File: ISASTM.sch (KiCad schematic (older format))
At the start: 137 parts, among them J1 Bus_ISA_8bit, J2 USB_C_Receptacle_USB2.0, J3 Boot select, J4 USB_C_Receptacle_USB2.0, J5 TagConnect_TC2030_SWD, SW1 Reset, U1 STM32H743IITx, U10 SN74AVC8T245PW, U11 SN74AVC8T245PW, U12 SN74AVC8T245PW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

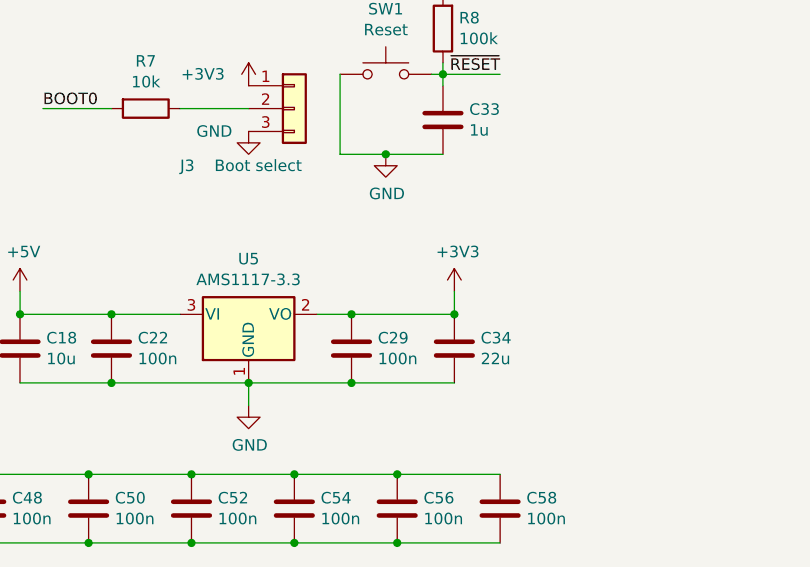
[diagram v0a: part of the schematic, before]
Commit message: Add 3v3 testpoint
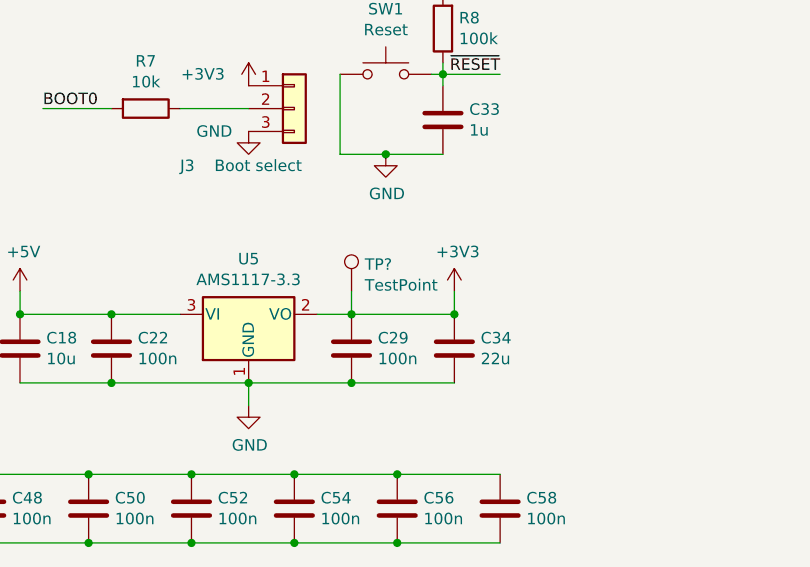
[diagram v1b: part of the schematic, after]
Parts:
- added TP?: TestPoint, TestPoint:TestPoint_Pad_2.0x2.0mm, symbol Connector:TestPoint
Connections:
- net +3V3: now also TP?.1
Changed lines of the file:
@@
 Text Label 1450 5400 0    50   ~ 0
 ~SPARE1_OE
+$Comp
+L Connector:TestPoint TP?
+U 1 1 625A8D11
+P 21850 10600
+F 0 "TP?" H 21908 10718 50  0000 L CNN
+F 1 "TestPoint" H 21908 10627 50  0000 L CNN
+F 2 "TestPoint:TestPoint_Pad_2.0x2.0mm" H 22050 10600 50  0001 C CNN
+F 3 "~" H 22050 10600 50  0001 C CNN
+	1    21850 10600
+	1    0    0    -1
+$EndComp
+Wire Wire Line
+	21850 10600 21850 10700
 $EndSCHEMATC

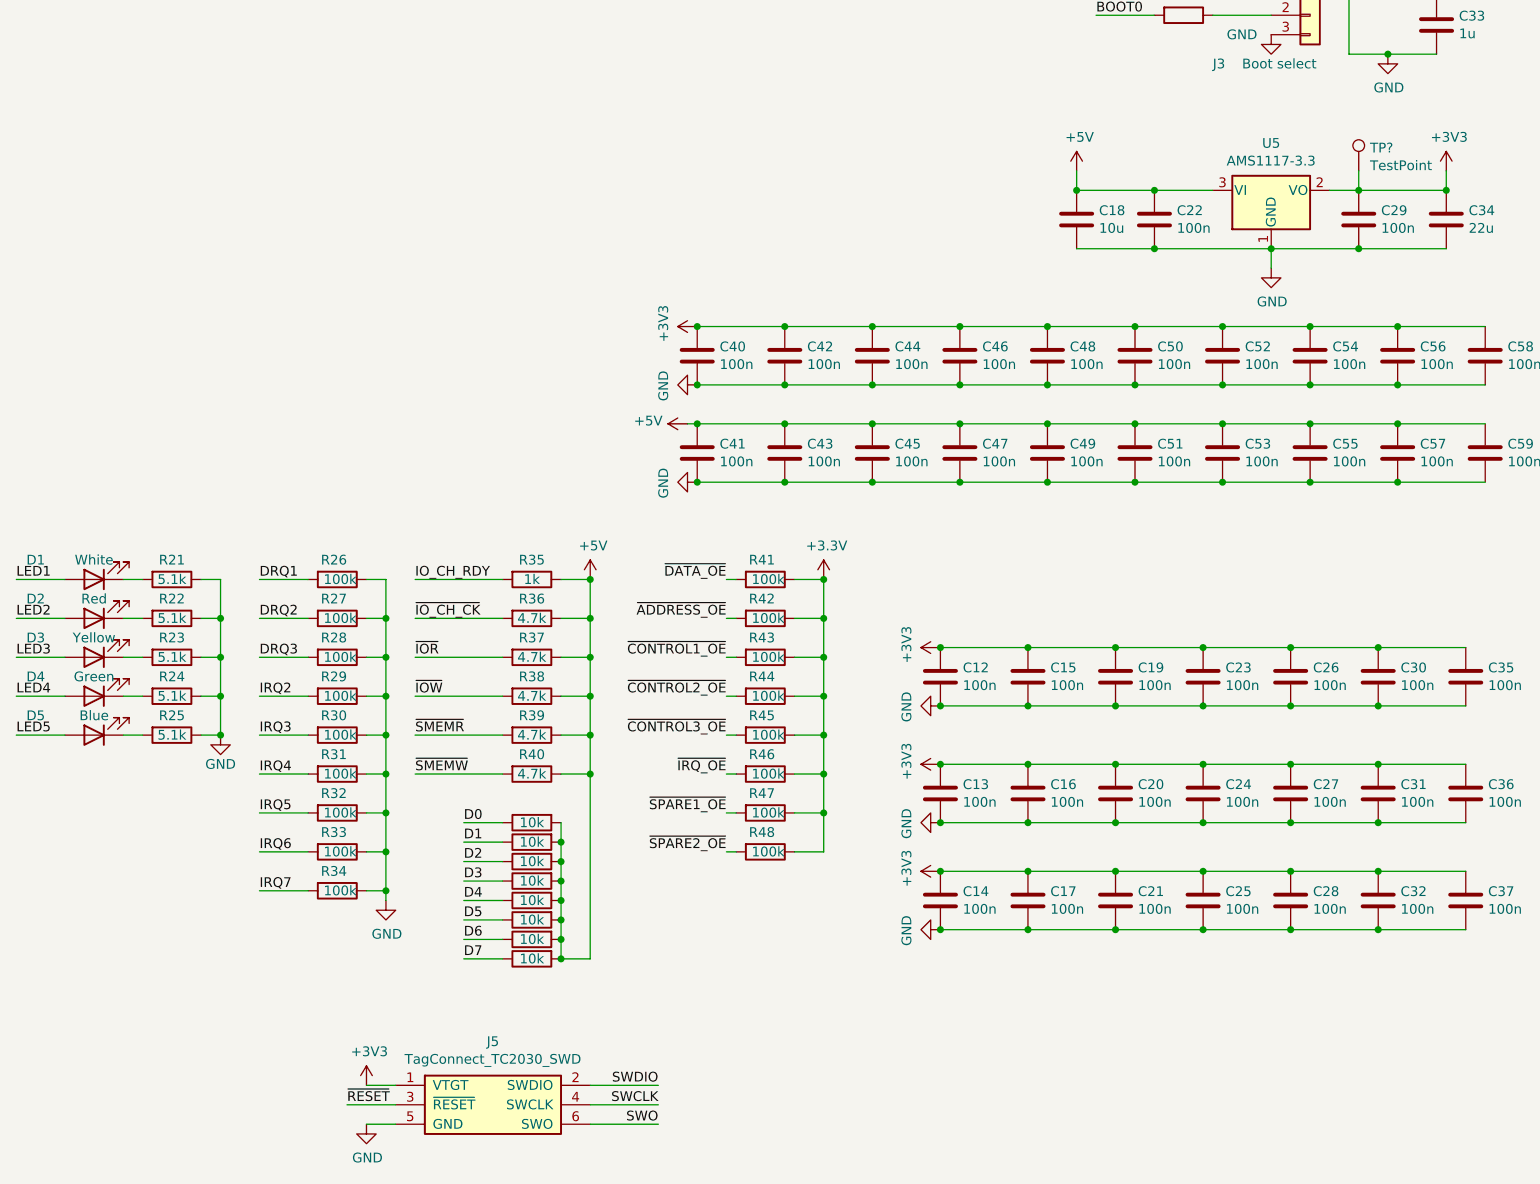
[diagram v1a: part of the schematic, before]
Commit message: Add tooling holes
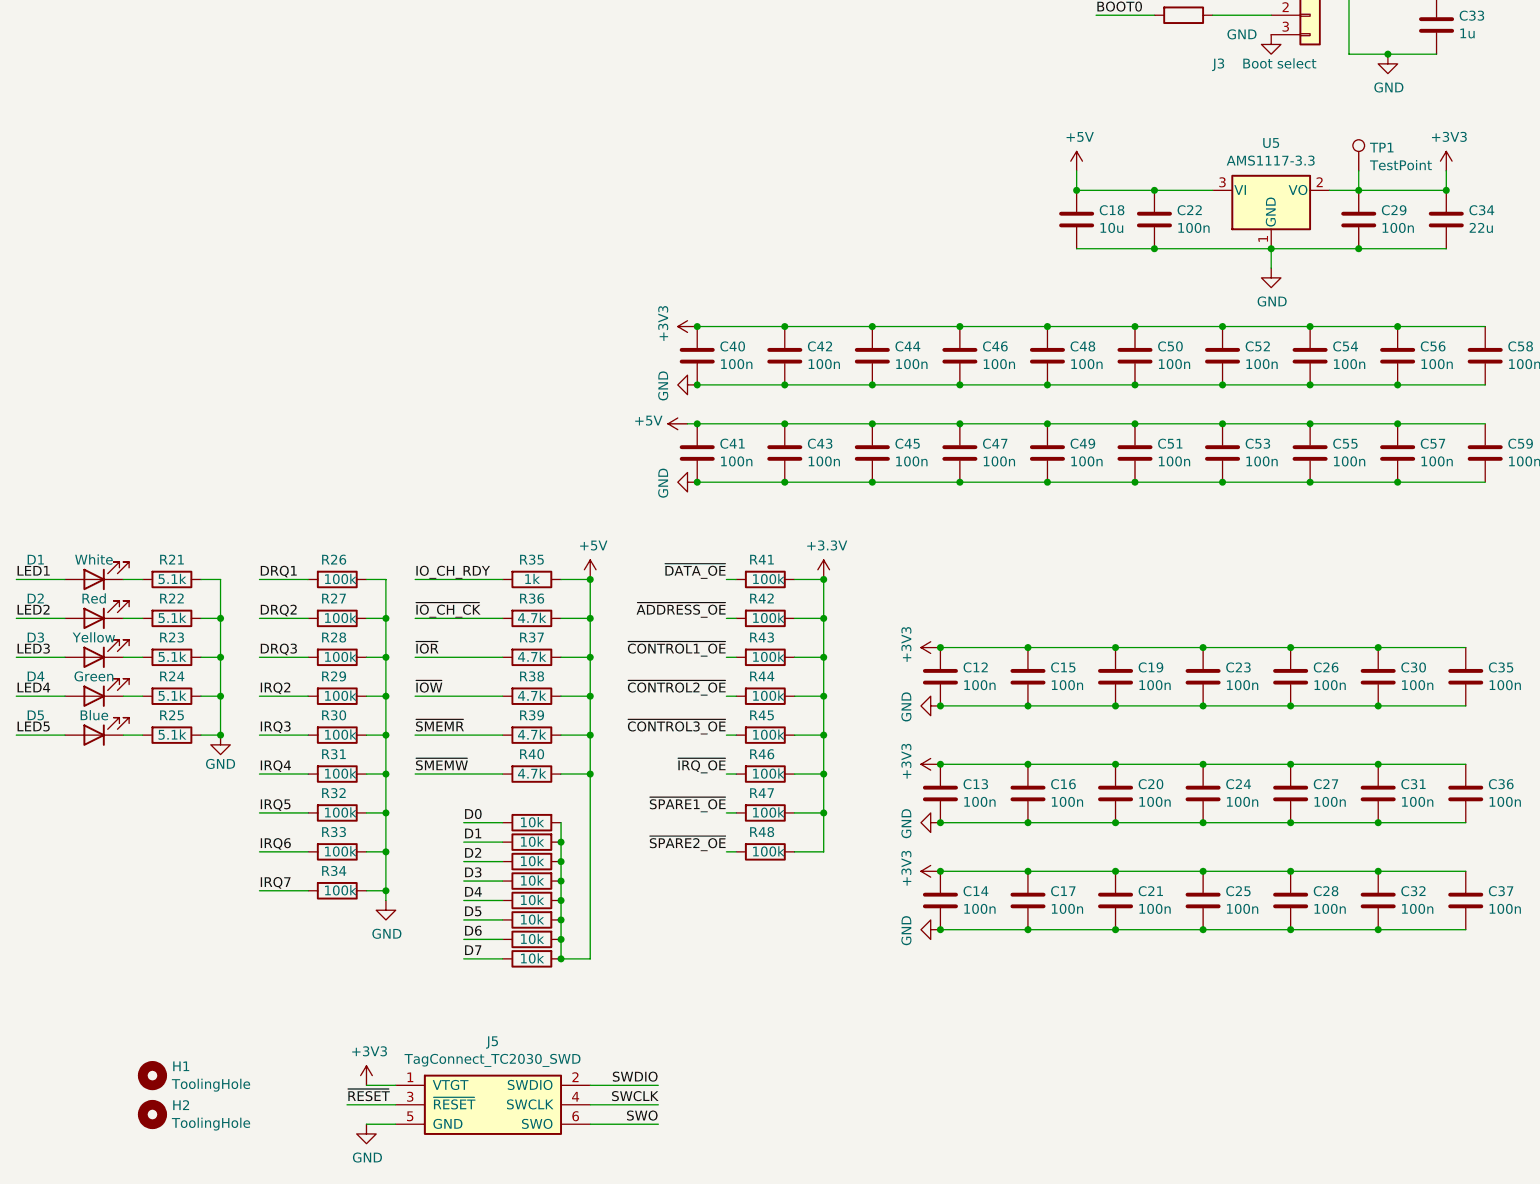
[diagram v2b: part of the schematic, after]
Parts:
- added H1, H2: ToolingHole, ISASTM:ToolingHole_JLCSMT, symbol Mechanical:MountingHole
- gave numbers to parts that had none: 1
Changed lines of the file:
@@
 ~SPARE1_OE
 $Comp
-L Connector:TestPoint TP?
+L Connector:TestPoint TP1
 U 1 1 625A8D11
 P 21850 10600
-F 0 "TP?" H 21908 10718 50  0000 L CNN
+F 0 "TP1" H 21908 10718 50  0000 L CNN
 F 1 "TestPoint" H 21908 10627 50  0000 L CNN
 F 2 "TestPoint:TestPoint_Pad_2.0x2.0mm" H 22050 10600 50  0001 C CNN
@@
 Wire Wire Line
 	21850 10600 21850 10700
+$Comp
+L Mechanical:MountingHole H1
+U 1 1 626BAFD0
+P 15650 15250
+F 0 "H1" H 15750 15296 50  0000 L CNN
+F 1 "ToolingHole" H 15750 15205 50  0000 L CNN
+F 2 "ISASTM:ToolingHole_JLCSMT" H 15650 15250 50  0001 C CNN
+F 3 "~" H 15650 15250 50  0001 C CNN
+	1    15650 15250
+	1    0    0    -1
+$EndComp
+$Comp
+L Mechanical:MountingHole H2
+U 1 1 5F7A598D
+P 15650 15450
+F 0 "H2" H 15750 15496 50  0000 L CNN
+F 1 "ToolingHole" H 15750 15405 50  0000 L CNN
+F 2 "ISASTM:ToolingHole_JLCSMT" H 15650 15450 50  0001 C CNN
+F 3 "~" H 15650 15450 50  0001 C CNN
+	1    15650 15450
+	1    0    0    -1
+$EndComp
 $EndSCHEMATC

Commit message: Fix missing ~REFRESH resistor, add better renders
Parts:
- added R49: 4.7k, Resistor_SMD:R_0402_1005Metric, symbol Device:R
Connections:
- net +5V: now also R49.1
- net ~REFRESH: now also R49.2
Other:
- note removed: "Refresh-Leitung braucht Pullup (und ist theoretisch bidirektional)\n"
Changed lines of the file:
@@
 Wire Wire Line
 	17450 4550 17950 4550
-Text Notes 23550 4250 0    197  ~ 0
-Refresh-Leitung braucht Pullup (und ist theoretisch bidirektional)\n
-Text Label 17250 14650 0    50   ~ 0
+Text Label 17250 14750 0    50   ~ 0
 D7
-Text Label 17250 14550 0    50   ~ 0
+Text Label 17250 14650 0    50   ~ 0
 D6
-Text Label 17250 14450 0    50   ~ 0
+Text Label 17250 14550 0    50   ~ 0
 D5
-Text Label 17250 14350 0    50   ~ 0
+Text Label 17250 14450 0    50   ~ 0
 D4
-Text Label 17250 14250 0    50   ~ 0
+Text Label 17250 14350 0    50   ~ 0
 D3
-Text Label 17250 14150 0    50   ~ 0
+Text Label 17250 14250 0    50   ~ 0
 D2
-Text Label 17250 14050 0    50   ~ 0
+Text Label 17250 14150 0    50   ~ 0
 D1
-Text Label 17250 13950 0    50   ~ 0
+Text Label 17250 14050 0    50   ~ 0
 D0
 Wire Wire Line
-	17450 13950 17250 13950
-Wire Wire Line
-	17250 14050 17450 14050
+	17450 14050 17250 14050
 Wire Wire Line
-	17450 14150 17250 14150
+	17250 14150 17450 14150
 Wire Wire Line
 	17450 14250 17250 14250
 Wire Wire Line
-	17250 14350 17450 14350
+	17450 14350 17250 14350
 Wire Wire Line
-	17450 14450 17250 14450
+	17250 14450 17450 14450
 Wire Wire Line
-	17250 14550 17450 14550
+	17450 14550 17250 14550
 Wire Wire Line
-	17450 14650 17250 14650
+	17250 14650 17450 14650
+Wire Wire Line
+	17450 14750 17250 14750
 $Comp
 L Device:R R?
 U 1 1 60585D61
-P 17600 13950
+P 17600 14050
 AR Path="/5F65970E/60585D61" Ref="R?"  Part="1"
 AR Path="/60585D61" Ref="R3"  Part="1"
-F 0 "R3" V 17393 13950 50  0001 C CNN
-F 1 "10k" V 17600 13950 50  0000 C CNN
-F 2 "Resistor_SMD:R_0402_1005Metric" V 17530 13950 50  0001 C CNN
-F 3 "~" H 17600 13950 50  0001 C CNN
-F 4 "C25744" V 17600 13950 50  0001 C CNN "LCSC"
-	1    17600 13950
-	0    -1   1    0
-$EndComp
-$Comp
-L Device:R R?
-U 1 1 6064A041
-P 17600 14050
-AR Path="/5F65970E/6064A041" Ref="R?"  Part="1"
-AR Path="/6064A041" Ref="R4"  Part="1"
-F 0 "R4" V 17393 14050 50  0001 C CNN
+F 0 "R3" V 17393 14050 50  0001 C CNN
 F 1 "10k" V 17600 14050 50  0000 C CNN
 F 2 "Resistor_SMD:R_0402_1005Metric" V 17530 14050 50  0001 C CNN
@@
 $Comp
 L Device:R R?
-U 1 1 606AB35D
+U 1 1 6064A041
 P 17600 14150
-AR Path="/5F65970E/606AB35D" Ref="R?"  Part="1"
-AR Path="/606AB35D" Ref="R5"  Part="1"
-F 0 "R5" V 17393 14150 50  0001 C CNN
+AR Path="/5F65970E/6064A041" Ref="R?"  Part="1"
+AR Path="/6064A041" Ref="R4"  Part="1"
+F 0 "R4" V 17393 14150 50  0001 C CNN
 F 1 "10k" V 17600 14150 50  0000 C CNN
 F 2 "Resistor_SMD:R_0402_1005Metric" V 17530 14150 50  0001 C CNN
@@
 $Comp
 L Device:R R?
-U 1 1 6070C66F
+U 1 1 606AB35D
 P 17600 14250
-AR Path="/5F65970E/6070C66F" Ref="R?"  Part="1"
-AR Path="/6070C66F" Ref="R6"  Part="1"
-F 0 "R6" V 17393 14250 50  0001 C CNN
+AR Path="/5F65970E/606AB35D" Ref="R?"  Part="1"
+AR Path="/606AB35D" Ref="R5"  Part="1"
+F 0 "R5" V 17393 14250 50  0001 C CNN
 F 1 "10k" V 17600 14250 50  0000 C CNN
 F 2 "Resistor_SMD:R_0402_1005Metric" V 17530 14250 50  0001 C CNN
@@
 $Comp
 L Device:R R?
-U 1 1 6076D981
+U 1 1 6070C66F
 P 17600 14350
-AR Path="/5F65970E/6076D981" Ref="R?"  Part="1"
-AR Path="/6076D981" Ref="R9"  Part="1"
-F 0 "R9" V 17393 14350 50  0001 C CNN
+AR Path="/5F65970E/6070C66F" Ref="R?"  Part="1"
+AR Path="/6070C66F" Ref="R6"  Part="1"
+F 0 "R6" V 17393 14350 50  0001 C CNN
 F 1 "10k" V 17600 14350 50  0000 C CNN
 F 2 "Resistor_SMD:R_0402_1005Metric" V 17530 14350 50  0001 C CNN
@@
 $Comp
 L Device:R R?
-U 1 1 607CEC43
+U 1 1 6076D981
 P 17600 14450
-AR Path="/5F65970E/607CEC43" Ref="R?"  Part="1"
-AR Path="/607CEC43" Ref="R10"  Part="1"
-F 0 "R10" V 17393 14450 50  0001 C CNN
+AR Path="/5F65970E/6076D981" Ref="R?"  Part="1"
+AR Path="/6076D981" Ref="R9"  Part="1"
+F 0 "R9" V 17393 14450 50  0001 C CNN
 F 1 "10k" V 17600 14450 50  0000 C CNN
 F 2 "Resistor_SMD:R_0402_1005Metric" V 17530 14450 50  0001 C CNN
@@
 $Comp
 L Device:R R?
-U 1 1 6082FF55
+U 1 1 607CEC43
 P 17600 14550
-AR Path="/5F65970E/6082FF55" Ref="R?"  Part="1"
-AR Path="/6082FF55" Ref="R11"  Part="1"
-F 0 "R11" V 17393 14550 50  0001 C CNN
+AR Path="/5F65970E/607CEC43" Ref="R?"  Part="1"
+AR Path="/607CEC43" Ref="R10"  Part="1"
+F 0 "R10" V 17393 14550 50  0001 C CNN
 F 1 "10k" V 17600 14550 50  0000 C CNN
 F 2 "Resistor_SMD:R_0402_1005Metric" V 17530 14550 50  0001 C CNN
@@
 $Comp
 L Device:R R?
-U 1 1 60891267
+U 1 1 6082FF55
 P 17600 14650
-AR Path="/5F65970E/60891267" Ref="R?"  Part="1"
-AR Path="/60891267" Ref="R12"  Part="1"
-F 0 "R12" V 17393 14650 50  0001 C CNN
+AR Path="/5F65970E/6082FF55" Ref="R?"  Part="1"
+AR Path="/6082FF55" Ref="R11"  Part="1"
+F 0 "R11" V 17393 14650 50  0001 C CNN
 F 1 "10k" V 17600 14650 50  0000 C CNN
 F 2 "Resistor_SMD:R_0402_1005Metric" V 17530 14650 50  0001 C CNN
@@
 	0    -1   1    0
 $EndComp
-Wire Wire Line
-	17750 14050 17750 14150
-Connection ~ 17750 14150
+$Comp
+L Device:R R?
+U 1 1 60891267
+P 17600 14750
+AR Path="/5F65970E/60891267" Ref="R?"  Part="1"
+AR Path="/60891267" Ref="R12"  Part="1"
+F 0 "R12" V 17393 14750 50  0001 C CNN
+F 1 "10k" V 17600 14750 50  0000 C CNN
+F 2 "Resistor_SMD:R_0402_1005Metric" V 17530 14750 50  0001 C CNN
+F 3 "~" H 17600 14750 50  0001 C CNN
+F 4 "C25744" V 17600 14750 50  0001 C CNN "LCSC"
+	1    17600 14750
+	0    -1   1    0
+$EndComp
 Wire Wire Line
 	17750 14150 17750 14250
@@
 Connection ~ 17750 14550
 Wire Wire Line
-	17750 13950 17750 14050
-Connection ~ 17750 14050
+	17750 14550 17750 14650
+Connection ~ 17750 14650
+Wire Wire Line
+	17750 14050 17750 14150
+Connection ~ 17750 14150
 Text Label 17150 3300 2    50   ~ 0
 ~SMEMW
@@
 Connection ~ 17900 12700
 Wire Wire Line
-	17900 14650 17750 14650
+	17900 14750 17750 14750
 Wire Wire Line
 	17900 13500 17900 13700
-Connection ~ 17900 13700
-Wire Wire Line
-	17900 13700 17900 14650
-Connection ~ 17750 14650
+Connection ~ 17750 14750
 Text Label 5500 3300 2    50   ~ 0
 ~REFRESH
@@
 Connection ~ 16850 13300
 Wire Wire Line
-	17750 14550 17750 14650
+	17750 14650 17750 14750
 $Comp
 L power:GND #PWR?
@@
 	1    0    0    -1
 $EndComp
+Text Label 17000 13900 0    50   ~ 0
+~REFRESH
+$Comp
+L Device:R R49
+U 1 1 5FABEBC9
+P 17600 13900
+F 0 "R49" V 17500 13900 50  0000 C CNN
+F 1 "4.7k" V 17600 13900 50  0000 C CNN
+F 2 "Resistor_SMD:R_0402_1005Metric" V 17530 13900 50  0001 C CNN
+F 3 "~" H 17600 13900 50  0001 C CNN
+F 4 "C25900" V 17600 13900 50  0001 C CNN "LCSC"
+	1    17600 13900
+	0    1    1    0
+$EndComp
+Wire Wire Line
+	17000 13900 17450 13900
+Wire Wire Line
+	17900 13900 17750 13900
+Wire Wire Line
+	17900 13700 17900 13900
+Connection ~ 17900 13700
+Connection ~ 17900 13900
+Wire Wire Line
+	17900 13900 17900 14750
 $EndSCHEMATC

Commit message: Add readme, schematic PDF, ibom, gerbers and change DRAM
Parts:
- U2: value MT48LC16M16A2P -> IS42S16160J-6TLI; LCSC C26393 -> C91278
- X1: value SG-7050CAN -> 14.31818 MHz; LCSC (none) -> C70517
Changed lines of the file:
@@
 AR Path="/5F6CD31D" Ref="U2"  Part="1"
 F 0 "U2" H 2350 14431 50  0000 C CNN
-F 1 "MT48LC16M16A2P" H 2350 14340 50  0000 C CNN
+F 1 "IS42S16160J-6TLI" H 2350 14340 50  0000 C CNN
 F 2 "Package_SO:TSOP-II-54_22.2x10.16mm_P0.8mm" H 2350 12950 50  0001 C CIN
-F 3 "https://datasheet.lcsc.com/szlcsc/Micron-Tech-MT48LC16M16A2P-6A-IT-G_C26393.pdf" H 2350 12700 50  0001 C CNN
-F 4 "C26393" H 2350 12950 50  0001 C CNN "LCSC"
+F 3 "" H 2350 12700 50  0001 C CNN
+F 4 "C91278" H 2350 12950 50  0001 C CNN "LCSC"
 	1    2350 12950
 	1    0    0    -1
@@
 P 17300 7500
 F 0 "X1" H 17000 7250 50  0000 L CNN
-F 1 "SG-7050CAN" H 17450 7250 50  0000 L CNN
+F 1 "14.31818 MHz" H 17450 7250 50  0000 L CNN
 F 2 "Oscillator:Oscillator_SMD_SeikoEpson_SG8002CA-4Pin_7.0x5.0mm" H 18000 7150 50  0001 C CNN
 F 3 "https://support.epson.biz/td/api/doc_check.php?dl=brief_SG7050CAN&lang=en" H 17200 7500 50  0001 C CNN
+F 4 "C70517" H 17300 7500 50  0001 C CNN "LCSC"
 	1    17300 7500
 	1    0    0    -1
